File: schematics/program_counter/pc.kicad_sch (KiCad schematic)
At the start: 17 parts, among them U1 74HC00, U2 74HC193, U3 74HC193, U4 74HC193, U5 74HC193, U6 74HC245, U7 74HC245

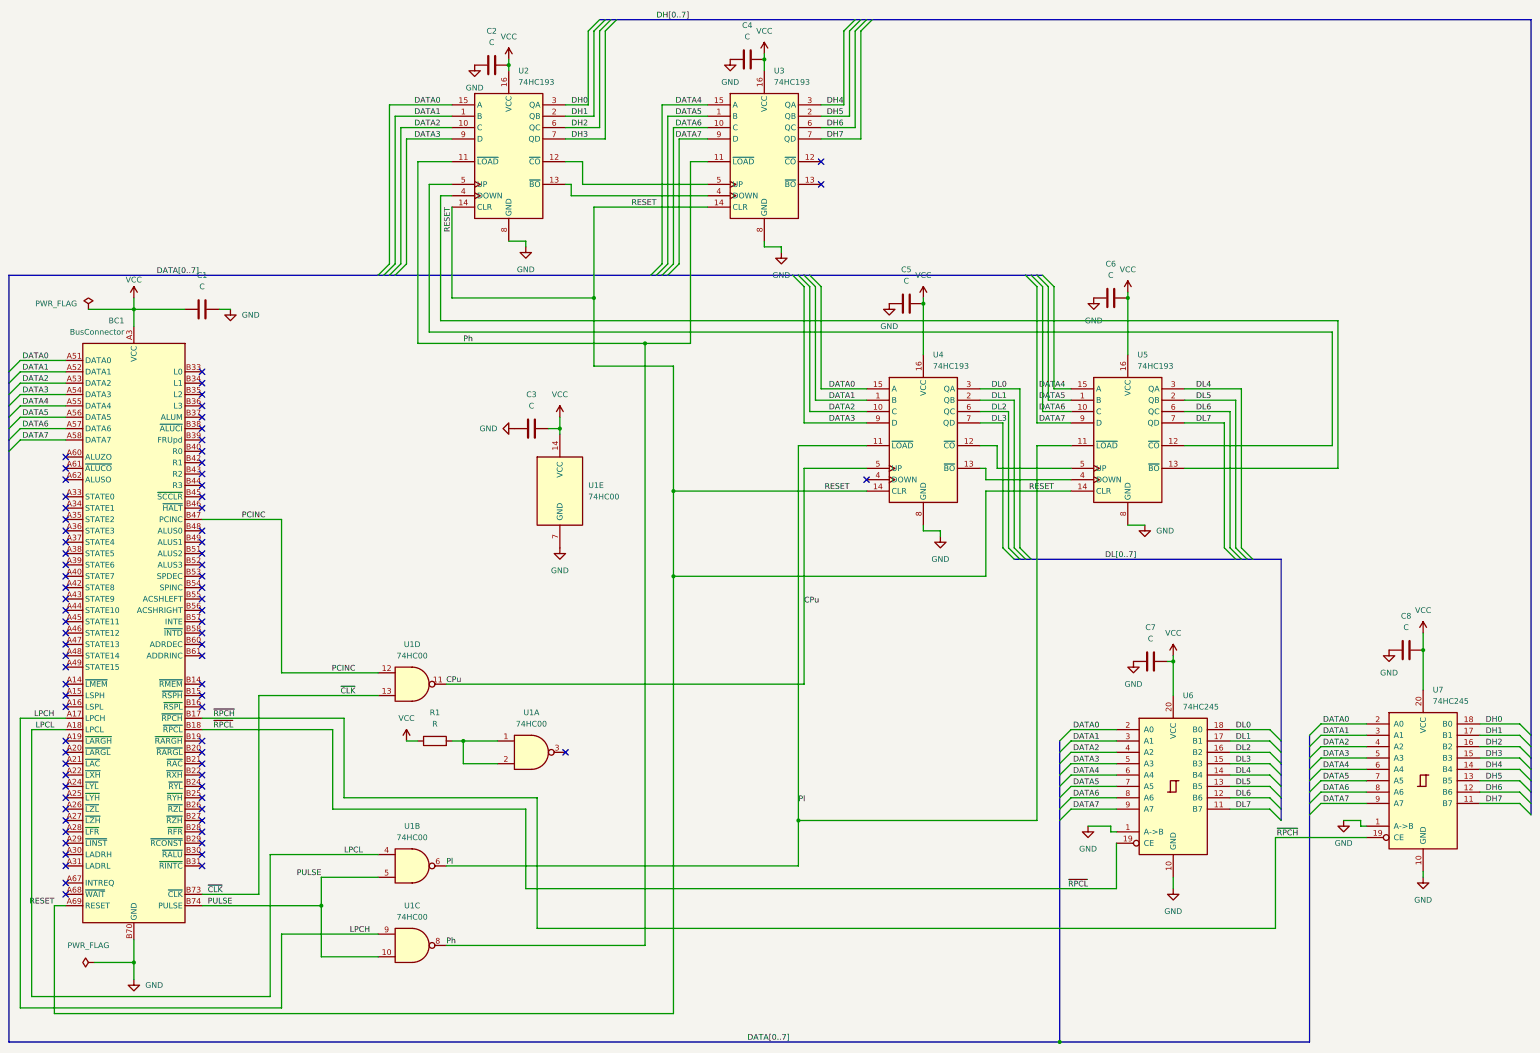
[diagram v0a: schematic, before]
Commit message: Add test points
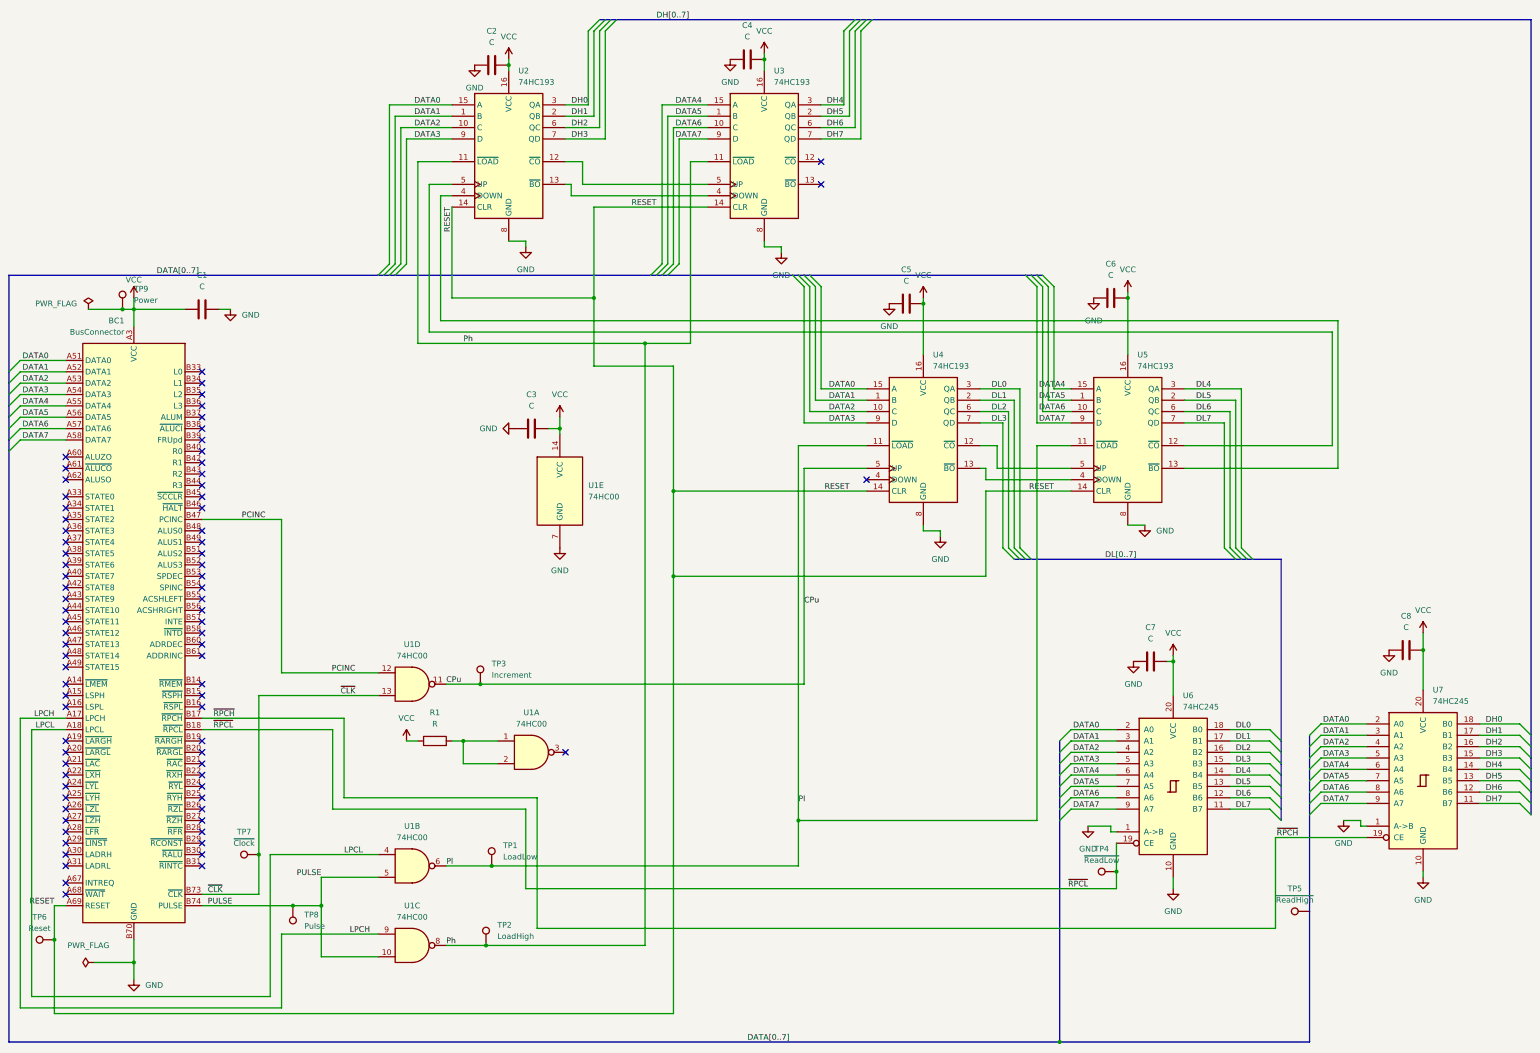
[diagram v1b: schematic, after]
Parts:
- added TP1: LoadLow, Connector_Pin:Pin_D1.0mm_L10.0mm, symbol Connector:TestPoint
- added TP2: LoadHigh, Connector_Pin:Pin_D1.0mm_L10.0mm, symbol Connector:TestPoint
- added TP3: Increment, Connector_Pin:Pin_D1.0mm_L10.0mm, symbol Connector:TestPoint
- added TP4: ~{ReadLow}, Connector_Pin:Pin_D1.0mm_L10.0mm, symbol Connector:TestPoint
- added TP5: ~{ReadHigh}, Connector_Pin:Pin_D1.0mm_L10.0mm, symbol Connector:TestPoint
- added TP6: Reset, Connector_Pin:Pin_D1.0mm_L10.0mm, symbol Connector:TestPoint
- added TP7: ~{Clock}, Connector_Pin:Pin_D1.0mm_L10.0mm, symbol Connector:TestPoint
- added TP8: Pulse, Connector_Pin:Pin_D1.0mm_L10.0mm, symbol Connector:TestPoint
- added TP9: Power, Connector_Pin:Pin_D1.0mm_L10.0mm, symbol Connector:TestPoint
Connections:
- net CPu: now also TP3.1
- net PULSE: now also TP8.1
- net Ph: now also TP2.1
- net Pl: now also TP1.1
- net RESET: now also TP6.1
- net VCC: now also TP9.1
- net ~{CLK}: now also TP7.1
- net ~{RPCL}: now also TP4.1

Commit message: test points sp and pc
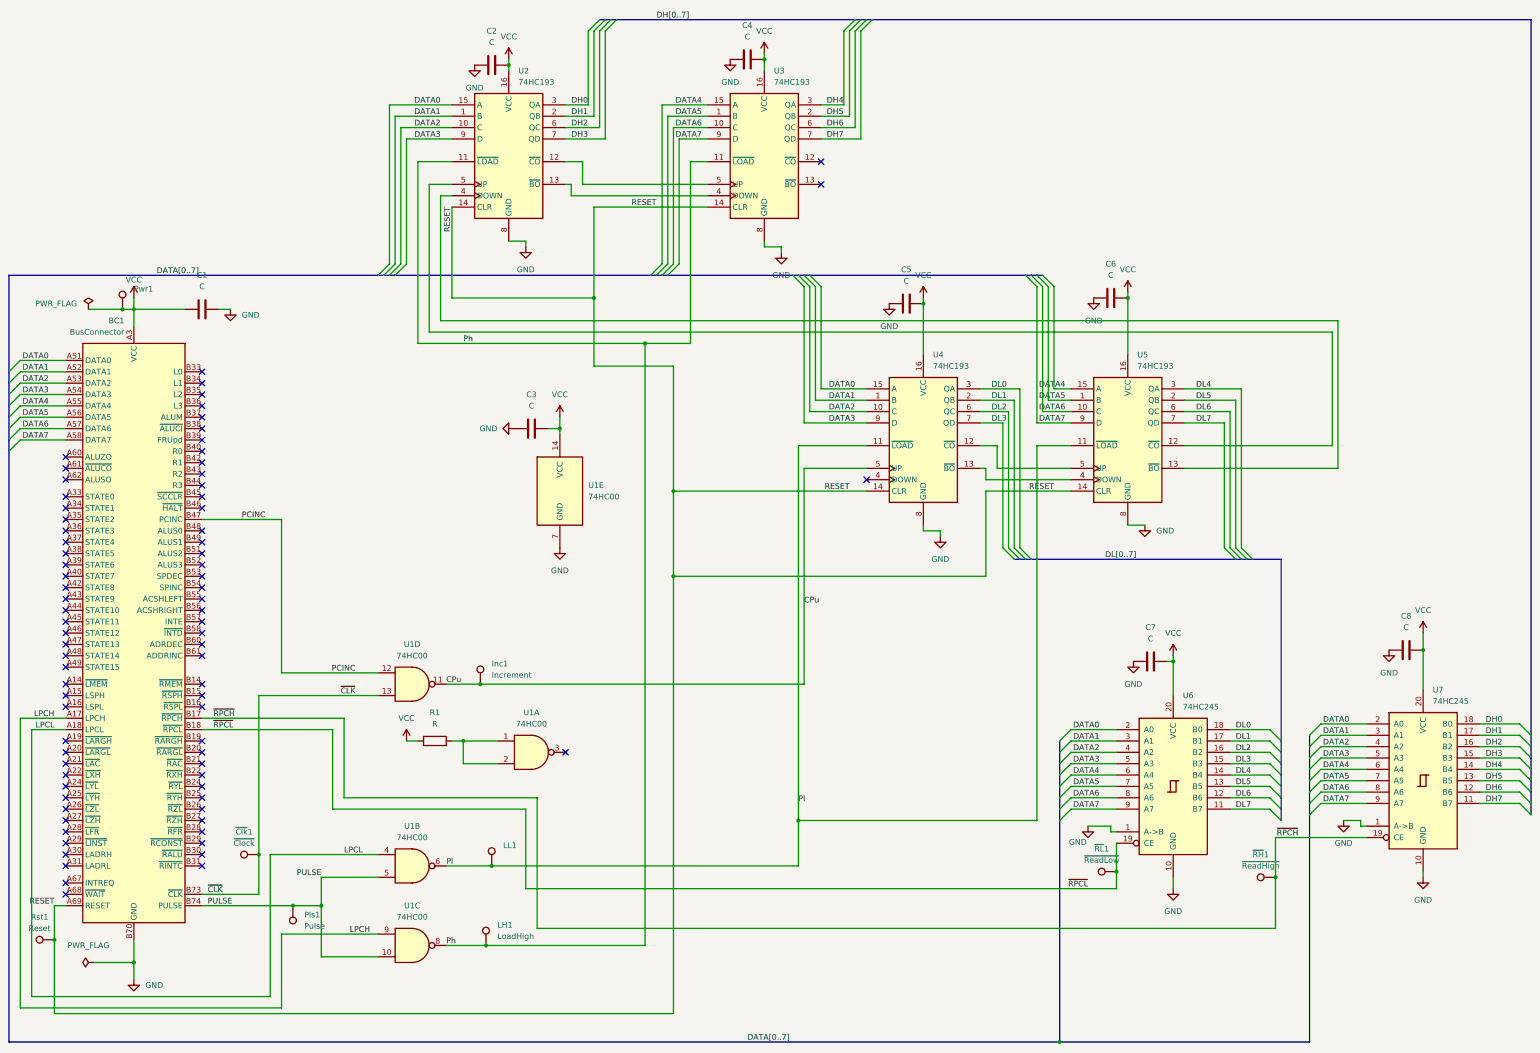
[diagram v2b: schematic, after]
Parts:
- removed TP5: ~{ReadHigh}, Connector_Pin:Pin_D1.0mm_L10.0mm, symbol Connector:TestPoint
- added ~{RH}1: ~{ReadHigh}, TestPoint:TestPoint_Pad_D1.0mm, symbol Connector:TestPoint
- Inc1: renamed from TP3; footprint Connector_Pin:Pin_D1.0mm_L10.0mm -> TestPoint:TestPoint_Pad_D1.0mm
- LH1: renamed from TP2; footprint Connector_Pin:Pin_D1.0mm_L10.0mm -> TestPoint:TestPoint_Pad_D1.0mm
- LL1: renamed from TP1; footprint Connector_Pin:Pin_D1.0mm_L10.0mm -> TestPoint:TestPoint_Pad_D1.0mm
- Pls1: renamed from TP8; footprint Connector_Pin:Pin_D1.0mm_L10.0mm -> TestPoint:TestPoint_Pad_D1.0mm
- Pwr1: renamed from TP9; footprint Connector_Pin:Pin_D1.0mm_L10.0mm -> TestPoint:TestPoint_Pad_D1.0mm
- Rst1: renamed from TP6; footprint Connector_Pin:Pin_D1.0mm_L10.0mm -> TestPoint:TestPoint_Pad_D1.0mm
- ~{Clk}1: renamed from TP7; footprint Connector_Pin:Pin_D1.0mm_L10.0mm -> TestPoint:TestPoint_Pad_D1.0mm
- ~{RL}1: renamed from TP4; footprint Connector_Pin:Pin_D1.0mm_L10.0mm -> TestPoint:TestPoint_Pad_D1.0mm
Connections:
- net ~{RPCH}: now also ~{RH}1.1
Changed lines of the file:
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@@
 	)
 	(junction
+		(at 328.93 209.55)
+		(diameter 0)
+		(color 0 0 0 0)
+	)
+	(junction
 		(at 157.48 27.94)
 		(diameter 0)
@@
 	(wire
 		(pts
-			(xy 328.93 220.98) (xy 328.93 200.66)
+			(xy 328.93 220.98) (xy 328.93 209.55)
 		)
 		(stroke
@@
 	(wire
 		(pts
+			(xy 328.93 209.55) (xy 328.93 200.66)
+		)
+		(stroke
+			(width 0)
+			(type default)
+		)
+	)
+	(wire
+		(pts
 			(xy 175.26 20.32) (xy 175.26 36.83)
 		)
@@
 	)
 	(symbol
-		(lib_id "Connector:TestPoint")
-		(at 336.55 217.17 90)
-		(unit 1)
-		(exclude_from_sim no)
-		(in_bom yes)
-		(on_board yes)
-		(dnp no)
-		(fields_autoplaced yes)
-		(property "Reference" "TP5"
-			(at 333.248 212.09 90)
-			(effects
-				(font
-					(size 1.27 1.27)
-				)
-			)
-		)
-		(property "Value" "~{ReadHigh}"
-			(at 333.248 214.63 90)
-			(effects
-				(font
-					(size 1.27 1.27)
-				)
-			)
-		)
-		(property "Footprint" "Connector_Pin:Pin_D1.0mm_L10.0mm"
-			(at 336.55 212.09 0)
-			(effects
-				(font
-					(size 1.27 1.27)
-				)
-				(hide yes)
-			)
-		)
-		(property "Datasheet" "~"
-			(at 336.55 212.09 0)
-			(effects
-				(font
-					(size 1.27 1.27)
-				)
-				(hide yes)
-			)
-		)
-		(property "Description" "test point"
-			(at 336.55 217.17 0)
-			(effects
-				(font
-					(size 1.27 1.27)
-				)
-				(hide yes)
-			)
-		)
-		(pin "1"
-		)
-		(instances
-			(project "pc"
-				(path "/34f7239d-5890-443b-b0ee-b6e214f6aaae"
-					(reference "TP5")
-					(unit 1)
-				)
-			)
-		)
-	)
-	(symbol
 		(lib_id "power:GND")
 		(at 361.95 209.55 0)
@@
 		(dnp no)
 		(fields_autoplaced yes)
-		(property "Reference" "TP9"
+		(property "Reference" "Pwr1"
 			(at 73.66 77.9779 0)
 			(effects
@@
 				)
 				(justify left)
+				(hide yes)
 			)
 		)
-		(property "Footprint" "Connector_Pin:Pin_D1.0mm_L10.0mm"
+		(property "Footprint" "TestPoint:TestPoint_Pad_D1.0mm"
 			(at 76.2 82.55 0)
 			(effects
@@
 			(project "pc"
 				(path "/34f7239d-5890-443b-b0ee-b6e214f6aaae"
-					(reference "TP9")
+					(reference "Pwr1")
 					(unit 1)
 				)
@@
 		(dnp no)
 		(fields_autoplaced yes)
-		(property "Reference" "TP4"
+		(property "Reference" "~{RL}1"
 			(at 290.068 203.2 90)
 			(effects
@@
 			)
 		)
-		(property "Footprint" "Connector_Pin:Pin_D1.0mm_L10.0mm"
+		(property "Footprint" "TestPoint:TestPoint_Pad_D1.0mm"
 			(at 293.37 203.2 0)
 			(effects
@@
 			(project "pc"
 				(path "/34f7239d-5890-443b-b0ee-b6e214f6aaae"
-					(reference "TP4")
+					(reference "~{RL}1")
 					(unit 1)
 				)
@@
 		(dnp no)
 		(fields_autoplaced yes)
-		(property "Reference" "TP6"
+		(property "Reference" "Rst1"
 			(at 52.578 218.44 90)
 			(effects
@@
 			)
 		)
-		(property "Footprint" "Connector_Pin:Pin_D1.0mm_L10.0mm"
+		(property "Footprint" "TestPoint:TestPoint_Pad_D1.0mm"
 			(at 55.88 218.44 0)
 			(effects
@@
 			(project "pc"
 				(path "/34f7239d-5890-443b-b0ee-b6e214f6aaae"
-					(reference "TP6")
+					(reference "Rst1")
 					(unit 1)
 				)
@@
 		(dnp no)
 		(fields_autoplaced yes)
-		(property "Reference" "TP2"
+		(property "Reference" "LH1"
 			(at 154.94 220.2179 0)
 			(effects
@@
 			)
 		)
-		(property "Footprint" "Connector_Pin:Pin_D1.0mm_L10.0mm"
+		(property "Footprint" "TestPoint:TestPoint_Pad_D1.0mm"
 			(at 157.48 224.79 0)
 			(effects
@@
 			(project "pc"
 				(path "/34f7239d-5890-443b-b0ee-b6e214f6aaae"
-					(reference "TP2")
+					(reference "LH1")
 					(unit 1)
 				)
@@
 		(dnp no)
 		(fields_autoplaced yes)
-		(property "Reference" "TP1"
+		(property "Reference" "LL1"
 			(at 156.21 202.4379 0)
 			(effects
@@
 				)
 				(justify left)
+				(hide yes)
 			)
 		)
-		(property "Footprint" "Connector_Pin:Pin_D1.0mm_L10.0mm"
+		(property "Footprint" "TestPoint:TestPoint_Pad_D1.0mm"
 			(at 158.75 207.01 0)
 			(effects
@@
 			(project "pc"
 				(path "/34f7239d-5890-443b-b0ee-b6e214f6aaae"
-					(reference "TP1")
+					(reference "LL1")
 					(unit 1)
 				)
@@
 		(dnp no)
 		(fields_autoplaced yes)
-		(property "Reference" "TP7"
+		(property "Reference" "~{Clk}1"
 			(at 98.298 199.39 90)
 			(effects
@@
 			)
 		)
-		(property "Footprint" "Connector_Pin:Pin_D1.0mm_L10.0mm"
+		(property "Footprint" "TestPoint:TestPoint_Pad_D1.0mm"
 			(at 101.6 199.39 0)
 			(effects
@@
 			(project "pc"
 				(path "/34f7239d-5890-443b-b0ee-b6e214f6aaae"
-					(reference "TP7")
+					(reference "~{Clk}1")
 					(unit 1)
 				)
@@
 		(on_board yes)
 		(dnp no)
-		(fields_autoplaced yes)
 		(property "Reference" "#PWR042"
 			(at 287.02 204.47 0)
@@
 		)
 		(property "Value" "GND"
-			(at 287.02 203.2 0)
+			(at 284.734 201.676 0)
 			(effects
 				(font
@@
 		(dnp no)
 		(fields_autoplaced yes)
-		(property "Reference" "TP3"
+		(property "Reference" "Inc1"
 			(at 153.67 161.7979 0)
 			(effects
@@
 			)
 		)
-		(property "Footprint" "Connector_Pin:Pin_D1.0mm_L10.0mm"
+		(property "Footprint" "TestPoint:TestPoint_Pad_D1.0mm"
 			(at 156.21 166.37 0)
 			(effects
@@
 			(project "pc"
 				(path "/34f7239d-5890-443b-b0ee-b6e214f6aaae"
-					(reference "TP3")
+					(reference "Inc1")
 					(unit 1)
 				)
@@
 		(dnp no)
 		(fields_autoplaced yes)
-		(property "Reference" "TP8"
+		(property "Reference" "Pls1"
 			(at 111.76 217.9319 0)
 			(effects
@@
 			)
 		)
-		(property "Footprint" "Connector_Pin:Pin_D1.0mm_L10.0mm"
+		(property "Footprint" "TestPoint:TestPoint_Pad_D1.0mm"
 			(at 104.14 215.9 0)
 			(effects
@@
 			(project "pc"
 				(path "/34f7239d-5890-443b-b0ee-b6e214f6aaae"
-					(reference "TP8")
+					(reference "Pls1")
 					(unit 1)
 				)
@@
 					(unit 1)
 				)
+			)
+		)
+	)
+	(symbol
+		(lib_id "Connector:TestPoint")
+		(at 328.93 209.55 90)
+		(unit 1)
+		(exclude_from_sim no)
+		(in_bom yes)
+		(on_board yes)
+		(dnp no)
+		(fields_autoplaced yes)
+		(property "Reference" "~{RH}1"
+			(at 325.628 204.47 90)
+			(effects
+				(font
+					(size 1.27 1.27)
+				)
+			)
+		)
+		(property "Value" "~{ReadHigh}"
+			(at 325.628 207.01 90)
+			(effects
+				(font
+					(size 1.27 1.27)
+				)
+			)
+		)
+		(property "Footprint" "TestPoint:TestPoint_Pad_D1.0mm"
+			(at 328.93 204.47 0)
+			(effects
+				(font
+					(size 1.27 1.27)
+				)
+				(hide yes)
+			)
+		)
+		(property "Datasheet" "~"
+			(at 328.93 204.47 0)
+			(effects
+				(font
+					(size 1.27 1.27)
+				)
+				(hide yes)
+			)
+		)
+		(property "Description" "test point"
+			(at 328.93 209.55 0)
+			(effects
+				(font
+					(size 1.27 1.27)
+				)
+				(hide yes)
+			)
+		)
+		(pin "1"
+		)
+		(instances
+			(project "pc"
+				(path "/34f7239d-5890-443b-b0ee-b6e214f6aaae"
+					(reference "~{RH}1")
+					(unit 1)
+				)
